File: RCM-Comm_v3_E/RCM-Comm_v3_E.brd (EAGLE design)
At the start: 50.8 x 66 mm, 37 parts, among them J1 BLACKFIN_HEADER, J3 USB-MICROB, U1 LANTRONIX_XPICO

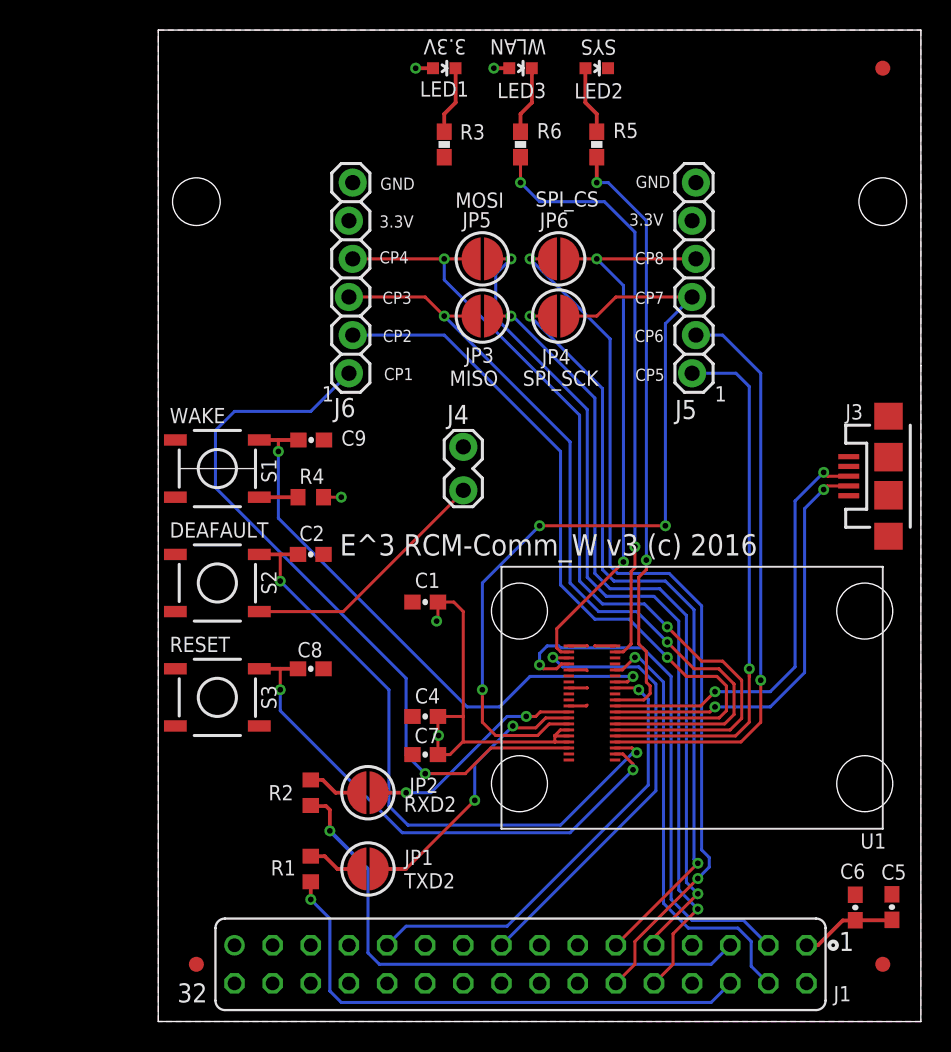
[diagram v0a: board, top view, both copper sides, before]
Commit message: Got Ethernet version of RCM-Comm_v3 board pretty much done. Out for Tim's review.
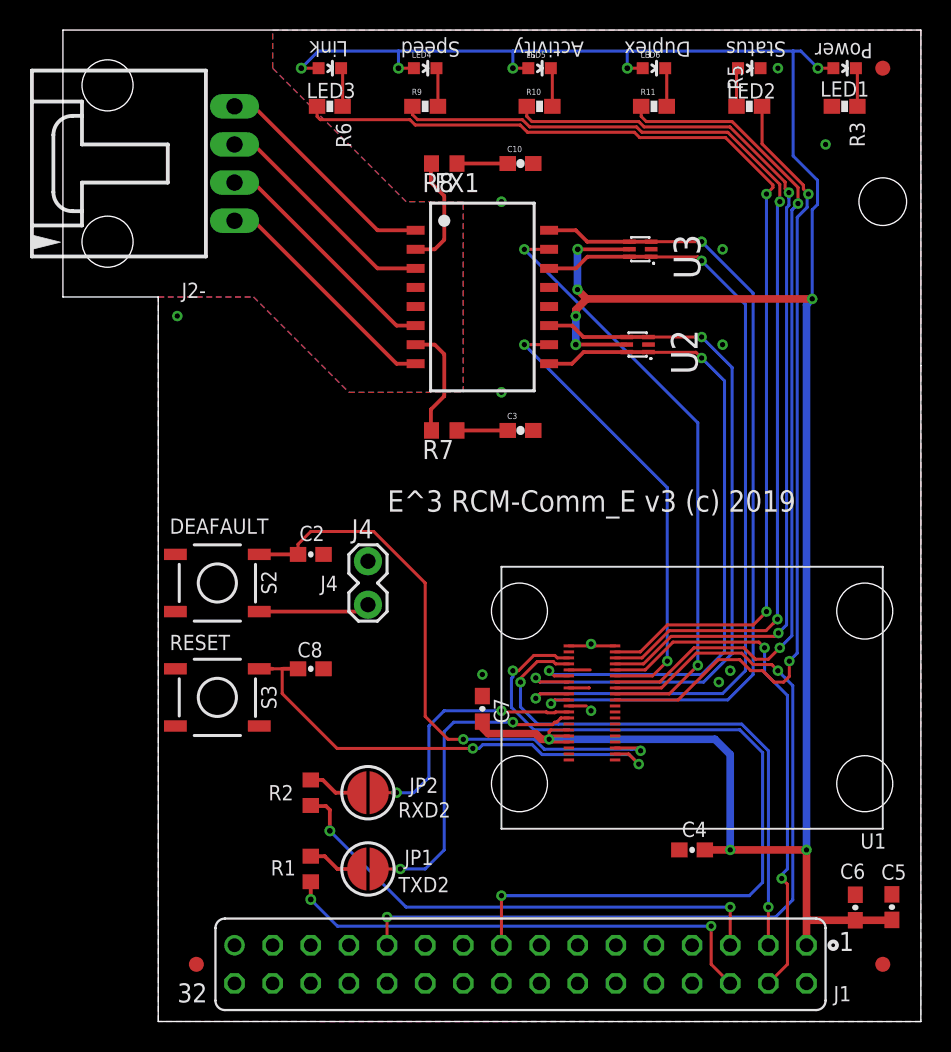
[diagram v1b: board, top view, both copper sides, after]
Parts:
- removed C1, C9: 0.1uF, SparkFun-Capacitors:0603-CAP
- removed J3: USB-MICROB, SparkFun-Connectors:USB-MICROB
- removed J5, J6: (no value), SparkFun-Connectors:1X06_LOCK
- removed JP3, JP4, JP5, JP6: JUMPER-PAD-2-NOROUND, SparkFun-Passives:PAD-JUMPER-2-NO_YES_SILK_ROUND
- removed R4: 1K, rcl:R0603
- removed S1: WAKE, SparkFun-Electromechanical:TACTILE-SWITCH-SMD
- added C10, C3: 0.01uF, 200V, spark_fun:0603-CAP
- added FX1: S558-5999-T7-F, halo-electronics:N5
- added J2-: C-GRID-04, MolexConnector:70555-04
- added LED4, LED5, LED6: GREEN, spark_fun:LED-0603
- added R10, R11, R9: 330, spark_fun:0603-RES
- added R7, R8: 75, rcl:R0603
- added U2, U3: RCLAMP0502A, SemtechRCLAMP:SC-89
- U1: value LANTRONIX_XPICO -> XPC10010MS-01; device xPico:LANTRONIX_XPICO -> xPicoEthernet:LANTRONIX_XPICO
- moved R3 26.8 mm to (48.3, 61.0), turned to 0 degrees
- moved LED1 26.7 mm to (48.3, 63.5)
- moved C4 19.9 mm to (38.1, 11.4)
- moved R6 13.0 mm to (14.0, 61.0), turned to 0 degrees
- moved LED3 12.7 mm to (14.0, 63.5)
- moved R5 10.5 mm to (41.9, 61.0), turned to 180 degrees
- moved LED2 10.2 mm to (41.9, 63.5)
- moved J4 9.92 mm to (16.5, 30.5)
- moved LOGO1 9.65 mm to (8.13, 38.2)
- moved U$3 9.56 mm to (9.91, 30.4)
- moved C7 4.88 mm to (24.1, 20.8), turned to 90 degrees
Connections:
- net N$24 renamed TXD2_J1
- net N$26 renamed RXD2_J1
- net WLAN_LED renamed LED1_LINK
- removed net BF_CLK: J1.11, JP4.1
- removed net BF_CS: J1.12, JP6.2
- removed net BF_MISO: J1.10, JP5.2
- removed net BF_MOSI: J1.9, JP3.1
- removed net CP1: J6.1, U1.P35
- removed net CP2/SPI_INT: J6.2, U1.P26
- removed net CP3/MISO: J6.3, JP3.2, U1.P28
- removed net CP4/MOSI: J6.4, JP5.1, U1.P30
- removed net CP5: J5.1, U1.P32
- removed net CP6: J5.2, U1.P34
- removed net CP7/SPI_SCK: J5.3, JP4.2, U1.P27
- removed net CP8/SPI_CS: J5.4, JP6.1, U1.P3
- removed net DDM: J3.D-, U1.P24
- removed net DDP: J3.D+, U1.P22
- removed net N$5: R4.2, S1.1
- removed net WKUP: C9.1, S1.3, U1.P14
- new net ERCT: FX1.15, U1.P18
- new net ERX+: FX1.16, U1.P19, U3.3, U3.4
- new net ERX-: FX1.14, U1.P17, U3.1, U3.6
- new net ETCT: FX1.10, U1.P12
- new net EXT+: FX1.11, U1.P13, U2.3, U2.4
- new net EXT-: FX1.9, U1.P11, U2.1, U2.6
- new net LED0_SPEED: R9.1, U1.P6
- new net LED2_ACTIVITY: R10.1, U1.P8
- new net LED3_DUPLEX: R11.1, U1.P14
- new net N$10: C3.1, R7.1
- new net N$11: FX1.7, R7.2
- new net N$14: LED6.C, R11.2
- new net N$15: LED5.C, R10.2
- new net N$16: LED4.C, R9.2
- new net N$7: FX1.2, R8.2
- new net N$9: C10.1, R8.1
- new net RX+: FX1.1, J2-.4
- new net RX-: FX1.3, J2-.3
- new net TX+: FX1.6, J2-.2
- new net TX-: FX1.8, J2-.1
- net GND: now also C10.2, C3.2, U2.2, U3.2; no longer C1.2, C9.2, J3.GND, J3.MT1, J3.MT2, J5.6, J6.6
- net VCC: now also LED4.A, LED5.A, LED6.A, U2.5, U3.5; no longer C1.1, J5.5, J6.5, R4.1
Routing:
- net VCC: track 37.5 -> 174.5 mm, vias 5 -> 13
- net LED0_SPEED: track 0.00 -> 67.9 mm, vias 0 -> 2
- net LED2_ACTIVITY: track 0.00 -> 61.9 mm, vias 0 -> 2
- net BF_CS: track 58.4 -> 0.00 mm, vias 2 -> 0
- net BF_MISO: track 58.0 -> 0.00 mm, vias 2 -> 0
- net CP4/MOSI: track 57.4 -> 0.00 mm, vias 2 -> 0
- net LED3_DUPLEX: track 0.00 -> 56.8 mm, vias 0 -> 2
- net ERX+: track 0.00 -> 56.3 mm, vias 0 -> 2
- net ERX-: track 0.00 -> 56.2 mm, vias 0 -> 2
- net CP7/SPI_SCK: track 53.6 -> 0.00 mm, vias 3 -> 0
- net CP3/MISO: track 53.3 -> 0.00 mm, vias 2 -> 0
- net BF_CLK: track 51.4 -> 0.00 mm, vias 2 -> 0
- net BF_MOSI: track 50.9 -> 0.00 mm, vias 2 -> 0
- net CP1: track 49.4 -> 0.00 mm, vias 1 -> 0
- net CP2/SPI_INT: track 49.0 -> 0.00 mm, vias 1 -> 0
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- added copper zone on layer 16, net GND
- removed copper zone on layer 16, net VCC
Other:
- board size 50.8 x 66 mm -> 57.2 x 66 mm
- board text added: "Activity"
- board text added: "Duplex"
- board text added: "E^3 RCM-Comm_E v3 (c) 2019"
- board text added: "Engineering^3, 2019 http://engineering3.org"
- board text added: "J4"
- board text added: "Link"
- board text added: "Power"
- board text added: "Speed"
- board text added: "Status"
- board text removed: "1"
- board text removed: "3.3V"
- board text removed: "CP1"
- board text removed: "CP2"
- board text removed: "CP3"
- board text removed: "CP4"
- board text removed: "CP5"
- board text removed: "CP6"
- board text removed: "CP7"
- board text removed: "CP8"
- board text removed: "E^3 RCM-Comm_W v3 (c) 2016"
- board text removed: "Engineering^3, 2016 http://engineering3.org"
- board text removed: "GND"
- board text removed: "MISO"
- board text removed: "MOSI"
- board text removed: "SPI_CS"
- board text removed: "SPI_SCK"
- board text removed: "SYS"
- board text removed: "WAKE"
- board text removed: "WLAN"
